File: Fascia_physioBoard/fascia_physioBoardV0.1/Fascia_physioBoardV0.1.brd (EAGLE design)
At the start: 37.3 x 39.1 mm, 89 parts, among them CN2 CA0612KRX7R9BB102, CN3 CA0612KRX7R9BB102, CN4 CA0612KRX7R9BB102, CN5 CA0612KRX7R9BB102, CN6 CA0612KRX7R9BB102, J1 MOLEX_52437-2471MOLEX_52437-2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, J2 MOLEX_52437-2471MOLEX_52437-2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, J3 MOLEX_51296-1294MOLEX_51296-1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, U1 ADS1299-X, U10 TPD4E1B06DCKR, U11 TPD4E1B06DCKR, U12 OPA320AIDBVRDBV5-L, U13 ADUM5028, U2 OPA2320AIDGKT_NOVA8-SOIC-L, U3 OPA2320AIDGKT_NOVAL8-SOIC-L, U4 HCNR200-300E, U5 OPA320AIDBVRDBV5-L, U6 TPD4E1B06DCKR, U7 TPD4E1B06DCKR, U8 TPD4E1B06DCKR, U9 TPD4E1B06DCKR

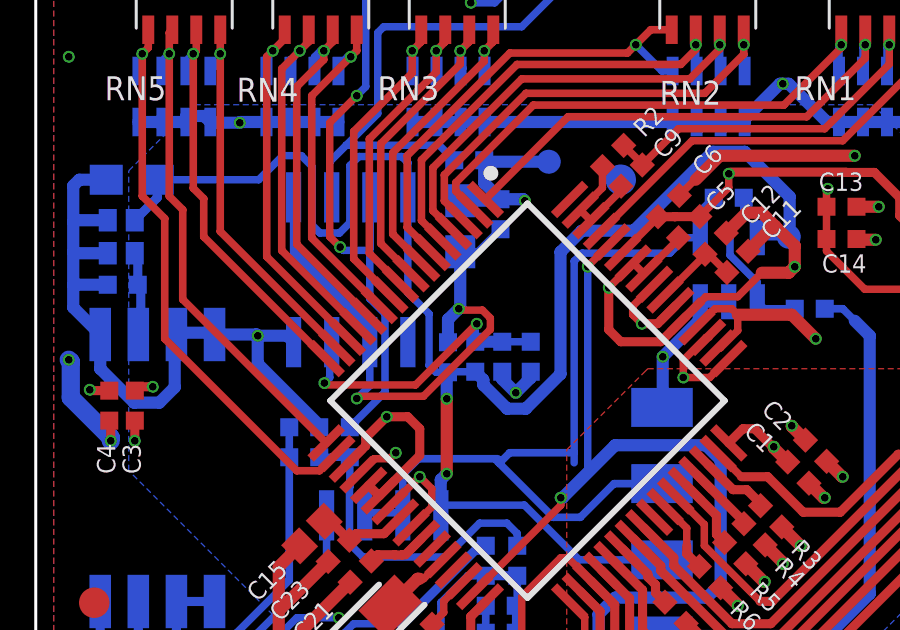
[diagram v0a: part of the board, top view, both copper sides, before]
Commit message: fixed issues related to missing traces from pin 1 to the feedback to pin 2
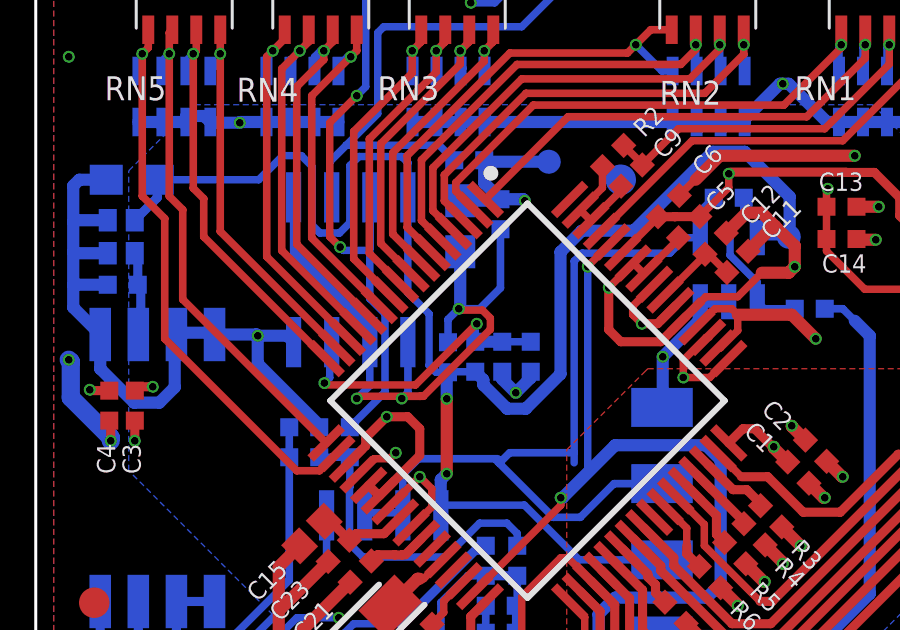
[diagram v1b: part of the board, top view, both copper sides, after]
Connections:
- removed net N$12: C24.2, C25.1, C27.1, U2.2, U2.5
- new net N$8: C24.2, C25.1, C27.1, U2.1, U2.2, U2.5
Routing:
- net N$8: track 0.00 -> 24.6 mm, vias 0 -> 3
- net N$12: track 19.9 -> 0.00 mm, vias 2 -> 0
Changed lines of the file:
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@@
 <drawing>
 <settings>
-<setting alwaysvectorfont="yes"/>
+<setting alwaysvectorfont="no"/>
 <setting verticaltext="up"/>
 </settings>
@@
 <wire x1="32.05" y1="9.55" x2="27.4682" y2="4.9682" width="0.3048" layer="1"/>
 </signal>
-<signal name="N$12">
-<contactref element="C24" pad="2"/>
-<contactref element="C25" pad="1"/>
-<contactref element="C27" pad="1"/>
-<contactref element="U2" pad="2"/>
-<contactref element="U2" pad="5"/>
-<wire x1="18.191" y1="18.55" x2="17.441" y2="17.8" width="0.25" layer="16"/>
-<wire x1="17.441" y1="17.8" x2="16.85" y2="17.8" width="0.25" layer="16"/>
-<wire x1="16.85" y1="17.8" x2="16.75" y2="17.7" width="0.25" layer="16"/>
-<wire x1="11.295" y1="19.613" x2="11.295" y2="17.805" width="0.25" layer="16"/>
-<wire x1="13.8" y1="15.3" x2="11.295" y2="17.805" width="0.25" layer="16"/>
-<wire x1="13.835" y1="14.787" x2="13.835" y2="13.335" width="0.25" layer="16"/>
-<wire x1="13.406325" y1="12.906325" x2="13.4" y2="12.906325" width="0.25" layer="16"/>
-<via x="13.4" y="12.906325" extent="1-16" drill="0.25"/>
-<wire x1="17.8532" y1="15.212275" x2="17.8532" y2="15.587725" width="0.25" layer="1"/>
-<wire x1="17.8532" y1="15.587725" x2="17.587725" y2="15.8532" width="0.25" layer="1"/>
-<wire x1="13.4" y1="12.906325" x2="13.4762" y2="12.982525" width="0.25" layer="1"/>
-<wire x1="17.587725" y1="15.8532" x2="16.8468" y2="15.8532" width="0.25" layer="1"/>
-<wire x1="16.8" y1="15.9" x2="16.8468" y2="15.8532" width="0.25" layer="1"/>
-<wire x1="13.4762" y1="12.982525" x2="15.62345" y2="12.982525" width="0.25" layer="1"/>
-<wire x1="15.62345" y1="12.982525" x2="17.8532" y2="15.212275" width="0.25" layer="1"/>
-<via x="16.8" y="15.9" extent="1-16" drill="0.25"/>
-<wire x1="13.835" y1="13.335" x2="13.406325" y2="12.906325" width="0.25" layer="16"/>
-<wire x1="16.85" y1="17.8" x2="16.85" y2="15.95" width="0.4064" layer="16"/>
-<wire x1="16.85" y1="15.95" x2="16.8" y2="15.9" width="0.4064" layer="16"/>
-<wire x1="16.8" y1="15.9" x2="16.442" y2="15.542" width="0.4064" layer="16"/>
-<wire x1="16.442" y1="15.542" x2="16.442" y2="14.781" width="0.4064" layer="16"/>
-<wire x1="13.835" y1="14.787" x2="13.8" y2="14.822" width="0.254" layer="16"/>
-<wire x1="13.8" y1="14.822" x2="13.8" y2="15.3" width="0.254" layer="16"/>
-</signal>
 <signal name="N$17">
 <contactref element="U1" pad="63"/>
@@
 <wire x1="25.446396875" y1="11.0740625" x2="26.220459375" y2="10.3" width="0.254" layer="1"/>
 </signal>
+<signal name="N$8">
+<contactref element="U2" pad="1"/>
+<contactref element="C24" pad="2"/>
+<contactref element="C25" pad="1"/>
+<contactref element="C27" pad="1"/>
+<contactref element="U2" pad="2"/>
+<contactref element="U2" pad="5"/>
+<wire x1="16.85" y1="17.8" x2="16.75" y2="17.7" width="0.25" layer="16"/>
+<wire x1="11.295" y1="19.613" x2="11.295" y2="17.805" width="0.25" layer="16"/>
+<wire x1="13.8" y1="15.3" x2="11.295" y2="17.805" width="0.25" layer="16"/>
+<wire x1="13.835" y1="14.787" x2="13.835" y2="13.335" width="0.25" layer="16"/>
+<wire x1="13.406325" y1="12.906325" x2="13.4" y2="12.906325" width="0.25" layer="16"/>
+<via x="13.4" y="12.906325" extent="1-16" drill="0.25"/>
+<wire x1="17.8532" y1="15.212275" x2="17.8532" y2="15.587725" width="0.25" layer="1"/>
+<wire x1="17.8532" y1="15.587725" x2="17.587725" y2="15.8532" width="0.25" layer="1"/>
+<wire x1="13.4" y1="12.906325" x2="13.4762" y2="12.982525" width="0.25" layer="1"/>
+<wire x1="17.587725" y1="15.8532" x2="16.8468" y2="15.8532" width="0.25" layer="1"/>
+<wire x1="16.8" y1="15.9" x2="16.8468" y2="15.8532" width="0.25" layer="1"/>
+<wire x1="13.4762" y1="12.982525" x2="15.62345" y2="12.982525" width="0.25" layer="1"/>
+<wire x1="15.62345" y1="12.982525" x2="17.8532" y2="15.212275" width="0.25" layer="1"/>
+<via x="16.8" y="15.9" extent="1-16" drill="0.25"/>
+<wire x1="13.835" y1="13.335" x2="13.406325" y2="12.906325" width="0.25" layer="16"/>
+<wire x1="16.85" y1="17.8" x2="16.85" y2="15.95" width="0.4064" layer="16"/>
+<wire x1="16.85" y1="15.95" x2="16.8" y2="15.9" width="0.4064" layer="16"/>
+<wire x1="13.835" y1="14.787" x2="13.8" y2="14.822" width="0.254" layer="16"/>
+<wire x1="13.8" y1="14.822" x2="13.8" y2="15.3" width="0.254" layer="16"/>
+<wire x1="18.191" y1="18.55" x2="18.191" y2="16.591" width="0.254" layer="16"/>
+<wire x1="18.191" y1="16.591" x2="17.5" y2="15.9" width="0.254" layer="16"/>
+<wire x1="17.5" y1="15.9" x2="16.9" y2="15.9" width="0.254" layer="16"/>
+<wire x1="16.9" y1="15.9" x2="16.85" y2="15.95" width="0.254" layer="16"/>
+<wire x1="16.8" y1="15.9" x2="16.442" y2="15.542" width="0.254" layer="16"/>
+<wire x1="16.442" y1="15.542" x2="16.442" y2="14.781" width="0.254" layer="16"/>
+<wire x1="15.105" y1="14.787" x2="15.105" y2="13.105" width="0.254" layer="16"/>
+<wire x1="15.105" y1="13.105" x2="14.9" y2="12.9" width="0.254" layer="16"/>
+<wire x1="14.9" y1="12.9" x2="14.9" y2="12.906321875" width="0.254" layer="16"/>
+<via x="14.9" y="12.906321875" extent="1-16" drill="0.25"/>
+<wire x1="14.9" y1="12.906321875" x2="14.9742" y2="12.980521875" width="0.254" layer="1"/>
+<wire x1="14.9742" y1="12.980521875" x2="15.516509375" y2="12.980521875" width="0.254" layer="1"/>
+<wire x1="15.516509375" y1="12.980521875" x2="15.5185125" y2="12.982525" width="0.254" layer="1"/>
+<wire x1="15.5185125" y1="12.982525" x2="15.62345" y2="12.982525" width="0.254" layer="1"/>
+</signal>
 </signals>

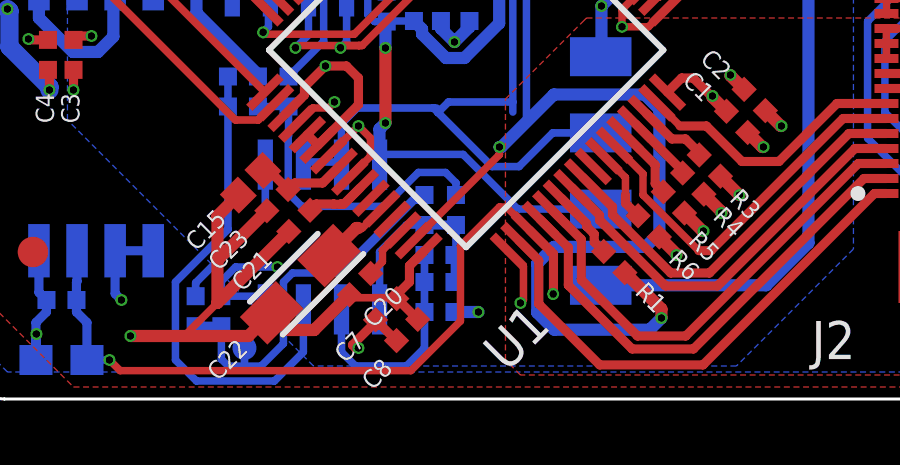
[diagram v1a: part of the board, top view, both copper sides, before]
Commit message: removed wrong component
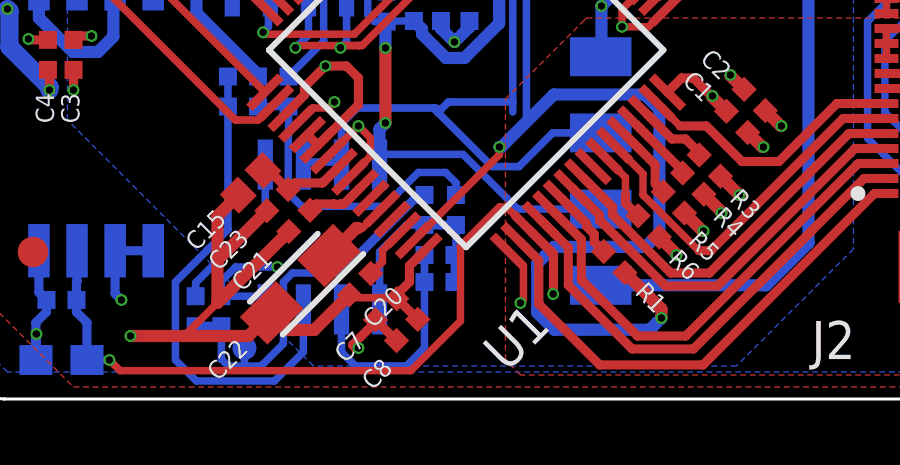
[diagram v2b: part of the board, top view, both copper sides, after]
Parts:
- removed R13: 10K, novaXR:0402-TIGHT
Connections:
- net GND_ISO: no longer R13.2
- net N$10: no longer R13.1
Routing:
- net GND_ISO: track 42.1 -> 41.3 mm, vias 6 -> 5
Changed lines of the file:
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@@
 <?xml version="1.0" encoding="utf-8"?>
 <!DOCTYPE eagle SYSTEM "eagle.dtd">
-<eagle version="9.4.2">
+<eagle version="9.5.1">
 <drawing>
 <settings>
@@
 <attribute name="VALUE" value="10K" x="18.2" y="5.862" size="0.6096" layer="28" font="vector" ratio="20" rot="MR180" align="top-center"/>
 </element>
-<element name="R13" library="novaXR" package="0402-TIGHT" value="10K" x="18.2" y="4.1" smashed="yes" rot="MR180">
-<attribute name="NAME" x="20" y="4.338" size="0.6096" layer="26" font="vector" ratio="20" rot="MR180" align="bottom-center"/>
-<attribute name="VALUE" value="10K" x="18.2" y="4.862" size="0.6096" layer="28" font="vector" ratio="20" rot="MR180" align="top-center"/>
-</element>
 <element name="R14" library="novaXR" package="0402-TIGHT" value="110K" x="17.7" y="7.5" smashed="yes" rot="MR90">
 <attribute name="NAME" x="17.462" y="9.3" size="0.6096" layer="26" font="vector" ratio="20" rot="MR90" align="bottom-center"/>
@@
 <contactref element="R9" pad="1"/>
 <contactref element="GND_ISO" pad="X"/>
-<contactref element="R13" pad="2"/>
 <contactref element="U2" pad="4"/>
 <contactref element="U3" pad="4"/>
@@
 <via x="10.1" y="15" extent="1-16" drill="0.25"/>
 <via x="12.8" y="5.6" extent="1-16" drill="0.25"/>
-<via x="19.5" y="4.1" extent="1-16" drill="0.25"/>
-<wire x1="19.5" y1="4.1" x2="18.7" y2="4.1" width="0.4064" layer="16"/>
 <wire x1="11.295" y1="14.787" x2="11.082" y2="15" width="0.4064" layer="16"/>
 <wire x1="11.082" y1="15" x2="10.1" y2="15" width="0.4064" layer="16"/>
@@
 <contactref element="R12" pad="1"/>
 <contactref element="C29" pad="1"/>
-<contactref element="R13" pad="1"/>
 <wire x1="17.7" y1="6" x2="17.7" y2="5.1" width="0.254" layer="16"/>
-<wire x1="17.7" y1="5.1" x2="17.7" y2="4.1" width="0.254" layer="16"/>
 <wire x1="14.935" y1="4.187" x2="14.935" y2="2.765" width="0.254" layer="16"/>
 <wire x1="14.935" y1="2.765" x2="15.4" y2="2.3" width="0.254" layer="16"/>
 <wire x1="15.4" y1="2.3" x2="17.1" y2="2.3" width="0.254" layer="16"/>
-<wire x1="17.7" y1="2.9" x2="17.7" y2="4.1" width="0.254" layer="16"/>
 <wire x1="17.1" y1="2.3" x2="17.7" y2="2.9" width="0.254" layer="16"/>
+<wire x1="17.7" y1="2.9" x2="17.7" y2="5.1" width="0.25" layer="16"/>
 </signal>
 <signal name="N$11">
